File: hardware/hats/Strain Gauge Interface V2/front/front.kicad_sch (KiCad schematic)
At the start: 76 parts, among them J1 Conn_01x14, U1 ADS1235IRHBT, U2 ADS1235IRHBT, U3 LMR50410Y5FQDBVRQ1, U5 BD450, U6 BD433

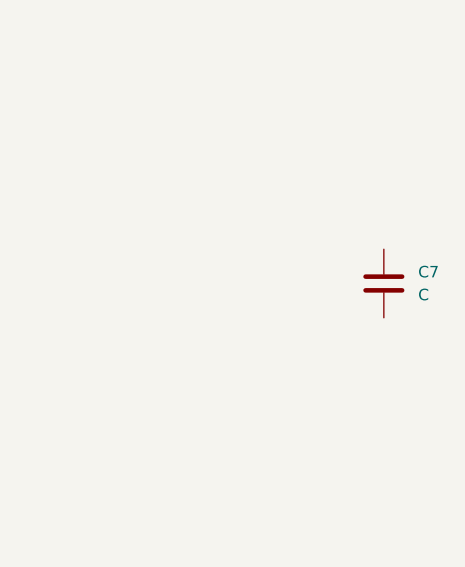
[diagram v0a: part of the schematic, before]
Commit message: pull AINBs to 3V3
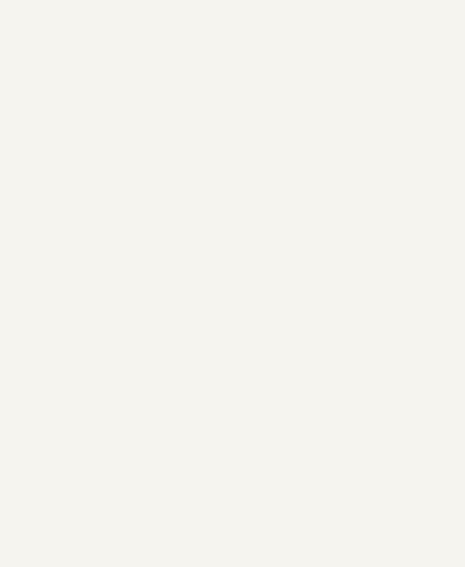
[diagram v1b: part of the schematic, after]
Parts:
- removed C7: C, symbol Device:C
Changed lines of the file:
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@@
-	)
-	(symbol
-		(lib_id "Device:C")
-		(at 421.64 102.87 0)
-		(unit 1)
-		(body_style 1)
-		(exclude_from_sim no)
-		(in_bom yes)
-		(on_board yes)
-		(in_pos_files yes)
-		(dnp no)
-		(fields_autoplaced yes)
-		(property "Reference" "C7"
-			(at 425.45 101.5999 0)
-			(show_name no)
-			(do_not_autoplace no)
-			(effects
-				(font
-					(size 1.27 1.27)
-				)
-				(justify left)
-			)
-		)
-		(property "Value" "C"
-			(at 425.45 104.1399 0)
-			(show_name no)
-			(do_not_autoplace no)
-			(effects
-				(font
-					(size 1.27 1.27)
-				)
-				(justify left)
-			)
-		)
-		(property "Footprint" ""
-			(at 422.6052 106.68 0)
-			(hide yes)
-			(show_name no)
-			(do_not_autoplace no)
-			(effects
-				(font
-					(size 1.27 1.27)
-				)
-			)
-		)
-		(property "Datasheet" ""
-			(at 421.64 102.87 0)
-			(hide yes)
-			(show_name no)
-			(do_not_autoplace no)
-			(effects
-				(font
-					(size 1.27 1.27)
-				)
-			)
-		)
-		(property "Description" "Unpolarized capacitor"
-			(at 421.64 102.87 0)
-			(hide yes)
-			(show_name no)
-			(do_not_autoplace no)
-			(effects
-				(font
-					(size 1.27 1.27)
-				)
-			)
-		)
-		(pin "1"
-		)
-		(pin "2"
-		)
-		(instances
-			(project "front"
-				(path "/bf4f6065-8f63-4b86-96d7-14957e755ff4"
-					(reference "C7")
-					(unit 1)
-				)
-			)
-		)
 	)
 	(symbol

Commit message: change switching reg to adjustable
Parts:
- U3: value LMR50410Y5FQDBVRQ1 -> LMR50410YQDBVRQ1
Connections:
- net +3V3: now also U2.25 (AIN5), U2.26 (AIN4), U2.27 (AIN3), U2.28 (AIN2)
- net +5V: no longer U2.25 (AIN5), U2.26 (AIN4), U2.27 (AIN3), U2.28 (AIN2)
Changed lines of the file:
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@@
 			)
 		)
-		(property "Value" "+5V"
+		(property "Value" "+3V3"
 			(at 119.38 209.5499 90)
 			(show_name no)
@@
 			)
 		)
-		(property "Value" "LMR50410Y5FQDBVRQ1"
+		(property "Value" "LMR50410YQDBVRQ1"
 			(at 48.26 29.21 0)
 			(show_name no)

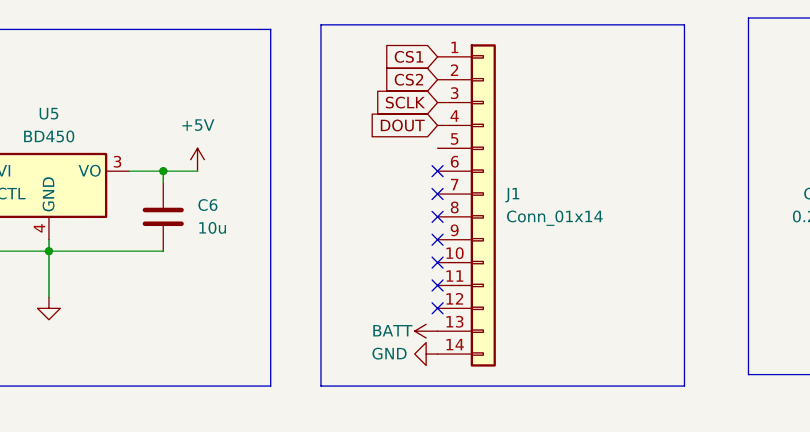
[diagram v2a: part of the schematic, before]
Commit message: add all footprints
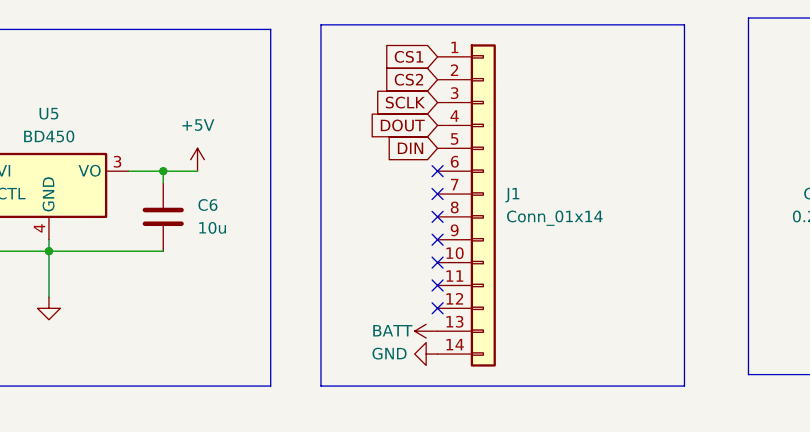
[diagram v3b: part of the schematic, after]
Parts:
- C10, C11, C12, C13, C14, C15, C16, C17, C18, C19, C20, C21, C22, C23, C24, C25, C26, C27, C28, C29, C30, C31, C32, C35, C36, C37, C8, C9: footprint (none) -> Capacitor_SMD:C_0603_1608Metric
- R1, R10, R11, R12, R13, R14, R15, R16, R17, R18, R19, R2, R20, R21, R22, R23, R24, R3, R4, R5, R6, R7, R8, R9: footprint (none) -> Resistor_SMD:R_0603_1608Metric
- SG1, SG2, SG3, SG4, SG5, SG6, SG7, SG8: footprint (none) -> Connector_JST:JST_XA_S02B-XASK-1_1x02_P2.50mm_Horizontal
- U1, U2: footprint RHB32_TEX -> CustomFootprints:RHB32_TEX
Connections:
- net DIN: now also J1.5 (Pin_5)
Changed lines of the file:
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@@
 		)
 	)
+	(global_label "DIN"
+		(shape input)
+		(at 167.64 27.94 180)
+		(fields_autoplaced yes)
+		(effects
+			(font
+				(size 1.27 1.27)
+			)
+			(justify right)
+		)
+		(property "Intersheetrefs" "${INTERSHEET_REFS}"
+			(at 161.4495 27.94 0)
+			(hide yes)
+			(show_name no)
+			(do_not_autoplace no)
+			(effects
+				(font
+					(size 1.27 1.27)
+				)
+				(justify right)
+			)
+		)
+	)
 	(global_label "DOUT"
 		(shape input)
@@
 			)
 		)
-		(property "Footprint" ""
+		(property "Footprint" "Connector_JST:JST_XA_S02B-XASK-1_1x02_P2.50mm_Horizontal"
 			(at 238.252 91.44 0)
 			(hide yes)
@@
 			)
 		)
-		(property "Footprint" ""
+		(property "Footprint" "Capacitor_SMD:C_0603_1608Metric"
 			(at 207.9752 95.25 0)
 			(hide yes)
@@
 			)
 		)
-		(property "Footprint" "RHB32_TEX"
+		(property "Footprint" "CustomFootprints:RHB32_TEX"
 			(at 58.42 105.41 0)
 			(hide yes)
@@
 			)
 		)
-		(property "Footprint" ""
+		(property "Footprint" "Capacitor_SMD:C_0603_1608Metric"
 			(at 39.0652 120.65 0)
 			(hide yes)
@@
 			)
 		)
-		(property "Footprint" ""
+		(property "Footprint" "Capacitor_SMD:C_0603_1608Metric"
 			(at 133.0452 201.93 0)
 			(hide yes)
@@
 			)
 		)
-		(property "Footprint" ""
+		(property "Footprint" "Resistor_SMD:R_0603_1608Metric"
 			(at 240.03 85.598 0)
 			(hide yes)
@@
 			)
 		)
-		(property "Footprint" ""
+		(property "Footprint" "Capacitor_SMD:C_0603_1608Metric"
 			(at 204.1652 213.36 0)
 			(hide yes)
@@
 			)
 		)
-		(property "Footprint" ""
+		(property "Footprint" "Resistor_SMD:R_0603_1608Metric"
 			(at 232.41 172.212 0)
 			(hide yes)
@@
 			)
 		)
-		(property "Footprint" ""
+		(property "Footprint" "Capacitor_SMD:C_0603_1608Metric"
 			(at 133.0452 118.11 0)
 			(hide yes)
@@
 			)
 		)
-		(property "Footprint" ""
+		(property "Footprint" "Connector_JST:JST_XA_S02B-XASK-1_1x02_P2.50mm_Horizontal"
 			(at 234.188 83.82 0)
 			(hide yes)
@@
 			)
 		)
-		(property "Footprint" ""
+		(property "Footprint" "Resistor_SMD:R_0603_1608Metric"
 			(at 140.97 188.468 90)
 			(hide yes)
@@
 			)
 		)
-		(property "Footprint" ""
+		(property "Footprint" "Connector_JST:JST_XA_S02B-XASK-1_1x02_P2.50mm_Horizontal"
 			(at 234.188 124.46 0)
 			(hide yes)
@@
 			)
 		)
-		(property "Footprint" ""
+		(property "Footprint" "Resistor_SMD:R_0603_1608Metric"
 			(at 214.63 137.668 90)
 			(hide yes)
@@
 			)
 		)
-		(property "Footprint" ""
+		(property "Footprint" "Capacitor_SMD:C_0603_1608Metric"
 			(at 44.1452 233.68 0)
 			(hide yes)
@@
 			)
 		)
-		(property "Footprint" ""
+		(property "Footprint" "Resistor_SMD:R_0603_1608Metric"
 			(at 214.63 130.048 90)
 			(hide yes)
@@
 			)
 		)
-		(property "Footprint" ""
+		(property "Footprint" "Capacitor_SMD:C_0603_1608Metric"
 			(at 204.1652 128.27 0)
 			(hide yes)
@@
 			)
 		)
-		(property "Footprint" ""
+		(property "Footprint" "Resistor_SMD:R_0603_1608Metric"
 			(at 31.75 46.228 90)
 			(hide yes)
@@
 			)
 		)
-		(property "Footprint" ""
+		(property "Footprint" "Capacitor_SMD:C_0603_1608Metric"
 			(at 115.2652 153.67 0)
 			(hide yes)
@@
 			)
 		)
-		(property "Footprint" ""
+		(property "Footprint" "Resistor_SMD:R_0603_1608Metric"
 			(at 214.63 97.028 90)
 			(hide yes)
@@
 			)
 		)
-		(property "Footprint" ""
+		(property "Footprint" "Capacitor_SMD:C_0603_1608Metric"
 			(at 33.9852 204.47 0)
 			(hide yes)
@@
 			)
 		)
-		(property "Footprint" ""
+		(property "Footprint" "Resistor_SMD:R_0603_1608Metric"
 			(at 39.37 46.228 90)
 			(hide yes)
@@
 			)
 		)
-		(property "Footprint" ""
+		(property "Footprint" "Resistor_SMD:R_0603_1608Metric"
 			(at 240.03 126.238 0)
 			(hide yes)
@@
 			)
 		)
-		(property "Footprint" ""
+		(property "Footprint" "Connector_JST:JST_XA_S02B-XASK-1_1x02_P2.50mm_Horizontal"
 			(at 234.188 166.37 0)
 			(hide yes)
@@
 			)
 		)
-		(property "Footprint" ""
+		(property "Footprint" "Capacitor_SMD:C_0603_1608Metric"
 			(at 207.9752 177.8 0)
 			(hide yes)
@@
 			)
 		)
-		(property "Footprint" ""
+		(property "Footprint" "Capacitor_SMD:C_0603_1608Metric"
 			(at 39.0652 204.47 0)
 			(hide yes)
@@
 			)
 		)
-		(property "Footprint" ""
+		(property "Footprint" "Capacitor_SMD:C_0603_1608Metric"
 			(at 45.4152 194.31 0)
 			(hide yes)
@@
 			)
 		)
-		(property "Footprint" ""
+		(property "Footprint" "Capacitor_SMD:C_0603_1608Metric"
 			(at 133.0452 186.69 0)
 			(hide yes)
@@
 			)
 		)
-		(property "Footprint" ""
+		(property "Footprint" "Resistor_SMD:R_0603_1608Metric"
 			(at 214.63 222.758 90)
 			(hide yes)
@@
 			)
 		)
-		(property "Footprint" ""
+		(property "Footprint" "Connector_JST:JST_XA_S02B-XASK-1_1x02_P2.50mm_Horizontal"
 			(at 238.252 132.08 0)
 			(hide yes)
@@
 			)
 		)
-		(property "Footprint" ""
+		(property "Footprint" "Resistor_SMD:R_0603_1608Metric"
 			(at 214.63 89.408 90)
 			(hide yes)
@@
 			)
 		)
-		(property "Footprint" ""
+		(property "Footprint" "Capacitor_SMD:C_0603_1608Metric"
 			(at 207.9752 135.89 0)
 			(hide yes)
@@
 			)
 		)
-		(property "Footprint" ""
+		(property "Footprint" "Capacitor_SMD:C_0603_1608Metric"
 			(at 45.4152 110.49 0)
 			(hide yes)
@@
 			)
 		)
-		(property "Footprint" ""
+		(property "Footprint" "Resistor_SMD:R_0603_1608Metric"
 			(at 140.97 112.268 90)
 			(hide yes)
@@
 			)
 		)
-		(property "Footprint" ""
+		(property "Footprint" "Resistor_SMD:R_0603_1608Metric"
 			(at 232.41 215.392 0)
 			(hide yes)
@@
 			)
 		)
-		(property "Footprint" ""
+		(property "Footprint" "Resistor_SMD:R_0603_1608Metric"
 			(at 214.63 171.958 90)
 			(hide yes)
@@
 			)
 		)
-		(property "Footprint" ""
+		(property "Footprint" "Capacitor_SMD:C_0603_1608Metric"
 			(at 204.1652 143.51 0)
 			(hide yes)
@@
 			)
 		)
-		(property "Footprint" ""
+		(property "Footprint" "Resistor_SMD:R_0603_1608Metric"
 			(at 232.41 130.302 0)
 			(hide yes)
@@
 			)
 		)
-		(property "Footprint" ""
+		(property "Footprint" "Capacitor_SMD:C_0603_1608Metric"
 			(at 204.1652 87.63 0)
 			(hide yes)
@@
 			)
 		)
-		(property "Footprint" ""
+		(property "Footprint" "Resistor_SMD:R_0603_1608Metric"
 			(at 240.03 211.328 0)
 			(hide yes)
@@
 			)
 		)
-		(property "Footprint" ""
+		(property "Footprint" "Capacitor_SMD:C_0603_1608Metric"
 			(at 207.9752 220.98 0)
 			(hide yes)
@@
 			)
 		)
-		(property "Footprint" ""
+		(property "Footprint" "Capacitor_SMD:C_0603_1608Metric"
 			(at 44.1452 149.86 0)
 			(hide yes)
@@
 			)
 		)
-		(property "Footprint" ""
+		(property "Footprint" "Capacitor_SMD:C_0603_1608Metric"
 			(at 204.1652 102.87 0)
 			(hide yes)
@@
 			)
 		)
-		(property "Footprint" ""
+		(property "Footprint" "Capacitor_SMD:C_0603_1608Metric"
 			(at 204.1652 170.18 0)
 			(hide yes)
@@
 			)
 		)
-		(property "Footprint" ""
+		(property "Footprint" "Capacitor_SMD:C_0603_1608Metric"
 			(at 138.1252 194.31 0)
 			(hide yes)
@@
 			)
 		)
-		(property "Footprint" ""
+		(property "Footprint" "Resistor_SMD:R_0603_1608Metric"
 			(at 214.63 179.578 90)
 			(hide yes)
@@
 			)
 		)
-		(property "Footprint" ""
+		(property "Footprint" "Capacitor_SMD:C_0603_1608Metric"
 			(at 133.0452 102.87 0)
 			(hide yes)
@@
 			)
 		)
-		(property "Footprint" ""
+		(property "Footprint" "Resistor_SMD:R_0603_1608Metric"
 			(at 240.03 168.148 0)
 			(hide yes)
@@
 			)
 		)
-		(property "Footprint" ""
+		(property "Footprint" "Capacitor_SMD:C_0603_1608Metric"
 			(at 204.1652 228.6 0)
 			(hide yes)
@@
 			)
 		)
-		(property "Footprint" ""
+		(property "Footprint" "Resistor_SMD:R_0603_1608Metric"
 			(at 125.222 106.68 90)
 			(hide yes)
@@
 			)
 		)
-		(property "Footprint" ""
+		(property "Footprint" "Connector_JST:JST_XA_S02B-XASK-1_1x02_P2.50mm_Horizontal"
 			(at 234.188 209.55 0)
 			(hide yes)
@@
 			)
 		)
-		(property "Footprint" ""
+		(property "Footprint" "Capacitor_SMD:C_0603_1608Metric"
 			(at 138.1252 110.49 0)
 			(hide yes)
@@
 			)
 		)
-		(property "Footprint" ""
+		(property "Footprint" "Resistor_SMD:R_0603_1608Metric"
 			(at 140.97 104.648 90)
 			(hide yes)
@@
 			)
 		)
-		(property "Footprint" ""
+		(property "Footprint" "Connector_JST:JST_XA_S02B-XASK-1_1x02_P2.50mm_Horizontal"
 			(at 238.252 173.99 0)
 			(hide yes)
@@
 			)
 		)
-		(property "Footprint" ""
+		(property "Footprint" "Capacitor_SMD:C_0603_1608Metric"
 			(at 115.2652 237.49 0)
 			(hide yes)
@@
 			)
 		)
-		(property "Footprint" ""
+		(property "Footprint" "Resistor_SMD:R_0603_1608Metric"
 			(at 125.222 190.5 90)
 			(hide yes)
@@
 			)
 		)
-		(property "Footprint" "RHB32_TEX"
+		(property "Footprint" "CustomFootprints:RHB32_TEX"
 			(at 58.42 189.23 0)
 			(hide yes)
@@
 			)
 		)
-		(property "Footprint" ""
+		(property "Footprint" "Resistor_SMD:R_0603_1608Metric"
 			(at 214.63 215.138 90)
 			(hide yes)
@@
 			)
 		)
-		(property "Footprint" ""
+		(property "Footprint" "Capacitor_SMD:C_0603_1608Metric"
 			(at 204.1652 185.42 0)
 			(hide yes)
@@
 			)
 		)
-		(property "Footprint" ""
+		(property "Footprint" "Resistor_SMD:R_0603_1608Metric"
 			(at 232.41 89.662 0)
 			(hide yes)
@@
 			)
 		)
-		(property "Footprint" ""
+		(property "Footprint" "Connector_JST:JST_XA_S02B-XASK-1_1x02_P2.50mm_Horizontal"
 			(at 238.252 217.17 0)
 			(hide yes)
@@
 			)
 		)
-		(property "Footprint" ""
+		(property "Footprint" "Resistor_SMD:R_0603_1608Metric"
 			(at 140.97 196.088 90)
 			(hide yes)
@@
 			)
 		)
-		(property "Footprint" ""
+		(property "Footprint" "Capacitor_SMD:C_0603_1608Metric"
 			(at 33.9852 120.65 0)
 			(hide yes)

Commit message: this is worse than torture
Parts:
- removed J1: Conn_01x14, Connector_JST:JST_XA_S14B-XASK-1_1x14_P2.50mm_Horizontal, symbol Connector_Generic:Conn_01x14
- added C38, C39, C40, C41: 1nf, Capacitor_SMD:C_0603_1608Metric, symbol Device:C
- added C42, C43: 10nf, Capacitor_SMD:C_0603_1608Metric, symbol Device:C
- added J1, J2: Conn_01x07, Connector_JST:JST_XA_S07B-XASK-1_1x07_P2.50mm_Horizontal, symbol Connector_Generic:Conn_01x07
- added R25, R26, R27, R28: 100, Resistor_SMD:R_0603_1608Metric, symbol Device:R
- added R29, R30, R31, R32: 120, Resistor_SMD:R_0603_1608Metric, symbol Device:R_45deg
- added SG10, SG9: TOP, Connector_JST:JST_XA_S02B-XASK-1_1x02_P2.50mm_Horizontal, symbol Device:R_45deg
- added SG11, SG12: BOTTOM, Connector_JST:JST_XA_S02B-XASK-1_1x02_P2.50mm_Horizontal, symbol Device:R_45deg
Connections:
- net +3V3: now also R31.1, R32.1, SG10.2, SG9.2; no longer U2.25 (AIN5), U2.26 (AIN4), U2.27 (AIN3), U2.28 (AIN2)
- net BATT: now also J1.6 (Pin_6), J2.6 (Pin_6)
- net CS1: now also J1.1 (Pin_1), J2.1 (Pin_1)
- net CS2: now also J1.2 (Pin_2), J2.2 (Pin_2)
- net DIN: now also J1.5 (Pin_5), J2.5 (Pin_5)
- net DOUT: now also J1.4 (Pin_4), J2.4 (Pin_4)
- net GND: now also C38.1, C39.2, C40.1, C41.2, J1.7 (Pin_7), J2.7 (Pin_7), R29.1, R30.1, SG11.2, SG12.2
- net SCLK: now also J1.3 (Pin_3), J2.3 (Pin_3)
- new net: R28.2, R32.2, SG12.1
- new net: R25.2, R29.2, SG9.1
- new net: R27.2, R30.2, SG10.1
- new net: R26.2, R31.2, SG11.1
- new net AIN2_B: C41.1, C43.2, R28.1, U2.28 (AIN2)
- new net AIN3_B: C40.2, C43.1, R27.1, U2.27 (AIN3)
- new net AIN4_B: C39.1, C42.2, R26.1, U2.26 (AIN4)
- new net AIN5_B: C38.2, C42.1, R25.1, U2.25 (AIN5)
- no-connect marks 9 -> 2
